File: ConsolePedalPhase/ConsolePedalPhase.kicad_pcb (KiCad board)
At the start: 2 copper layers, 100 x 37 mm, 15 parts, among them J1 Conn_02x25_Counter_Clockwise, Q1 2N3904

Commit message: minor changes
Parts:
- removed D4: 1N914, Diode_SMD:D_SOD-323
- removed Distortion: 250K Distortion, Connector_PinSocket_2.54mm:PinSocket_1x03_P2.54mm_Vertical
- removed Q1: 2N3904, Package_TO_SOT_SMD:SOT-23
- removed REF** (x2): MountingHole_2.5mm_Pad, MountingHole:MountingHole_2.5mm_Pad
- removed Volume: 250K Volume, Connector_PinSocket_2.54mm:PinSocket_1x03_P2.54mm_Vertical
- added C10: 100uF, Capacitor_SMD:C_0603_1608Metric, F.Cu at (137.4, 77.5)
- added C11: 10uF, Capacitor_SMD:C_0603_1608Metric, F.Cu at (133.4, 80.0)
- added C12: 2.2nF, Capacitor_SMD:C_0603_1608Metric, F.Cu at (121.8, 86.1)
- added C13: 1nF, Capacitor_SMD:C_0603_1608Metric, F.Cu at (141.8, 73.6)
- added C14: 10nF, Capacitor_SMD:C_0603_1608Metric, F.Cu at (145.9, 74.4)
- added C15: 470pF, Capacitor_SMD:C_0603_1608Metric, F.Cu at (157.9, 74.8)
- added C16: 100nF, Capacitor_SMD:C_0603_1608Metric, F.Cu at (133.8, 82.5)
- added C17: 4.7nF, Capacitor_SMD:C_0603_1608Metric, F.Cu at (133.8, 85.0)
- added C18: 33nF, Capacitor_SMD:C_0603_1608Metric, F.Cu at (137.4, 80.0)
- added C19: 100nF, Capacitor_SMD:C_0603_1608Metric, F.Cu at (137.8, 82.5)
- added C3: 10nF, Capacitor_SMD:C_0603_1608Metric, F.Cu at (145.8, 87.0)
- added C4: 100nF, Capacitor_SMD:C_0603_1608Metric, F.Cu at (149.8, 84.5)
- added C5: 100uF, Capacitor_SMD:C_0603_1608Metric, F.Cu at (153.9, 74.8)
- added C6: 100nF, Capacitor_SMD:C_0603_1608Metric, F.Cu at (141.8, 71.1)
- added C7: 100nF, Capacitor_SMD:C_0603_1608Metric, F.Cu at (125.8, 86.1)
- added C8: 10nF, Capacitor_SMD:C_0603_1608Metric, F.Cu at (133.4, 77.5)
- added C9: 220nF, Capacitor_SMD:C_0603_1608Metric, F.Cu at (160.7, 56.0)
- added J2: AudioJack2, Connector_Audio:Jack_3.5mm_CUI_SJ1-3535NG_Horizontal, F.Cu at (173.4, 99.7)
- added R10: 470K, Resistor_SMD:R_0603_1608Metric, F.Cu at (141.8, 81.1)
- added R11: 10K, Resistor_SMD:R_0603_1608Metric, F.Cu at (156.8, 69.8)
- added R12: 10K, Resistor_SMD:R_0603_1608Metric, F.Cu at (141.8, 83.6)
- added R13: 22K, Resistor_SMD:R_0603_1608Metric, F.Cu at (145.8, 79.4)
- added R14: 22K, Resistor_SMD:R_0603_1608Metric, F.Cu at (149.9, 76.9)
- added R15: 330K, Resistor_SMD:R_0603_1608Metric, F.Cu at (160.7, 66.0)
- added R16: 330K, Resistor_SMD:R_0603_1608Metric, F.Cu at (153.9, 72.3)
- added R17: 100K, Resistor_SMD:R_0603_1608Metric, F.Cu at (145.8, 82.0)
- added R18: 4.7K, Resistor_SMD:R_0603_1608Metric, F.Cu at (141.8, 86.1)
- added R19: 39K, Resistor_SMD:R_0603_1608Metric, F.Cu at (160.7, 63.5)
- added R20: 100K, Resistor_SMD:R_0603_1608Metric, F.Cu at (160.8, 68.6)
- added R21: 330K, Resistor_SMD:R_0603_1608Metric, F.Cu at (149.9, 74.4)
- added R22: 10K, Resistor_SMD:R_0603_1608Metric, F.Cu at (157.9, 72.3)
- added R23: 100K, Resistor_SMD:R_0603_1608Metric, F.Cu at (149.8, 79.4)
- added R24: 10K, Resistor_SMD:R_0603_1608Metric, F.Cu at (149.8, 82.0)
- added R25: 10K, Resistor_SMD:R_0603_1608Metric, F.Cu at (153.9, 77.4)
- added R4: 100K, Resistor_SMD:R_0603_1608Metric, F.Cu at (152.8, 69.8)
- added R5: 100K, Resistor_SMD:R_0603_1608Metric, F.Cu at (160.7, 61.0)
- added R6: 10K, Resistor_SMD:R_0603_1608Metric, F.Cu at (145.9, 76.9)
- added R7: 4.7K, Resistor_SMD:R_0603_1608Metric, F.Cu at (129.8, 86.1)
- added R8: 100K, Resistor_SMD:R_0603_1608Metric, F.Cu at (145.8, 84.5)
- added R9: 100K, Resistor_SMD:R_0603_1608Metric, F.Cu at (137.8, 85.0)
- added RV1: 20K, Potentiometer_THT:Potentiometer_Alps_RK09L_Single_Vertical, F.Cu at (133.1, 64.8)
- added RV2: C100K, Potentiometer_THT:Potentiometer_Alps_RK09L_Single_Vertical, F.Cu at (118.3, 79.8)
- added RV3: 1M, Potentiometer_THT:Potentiometer_Alps_RK09L_Single_Vertical, F.Cu at (118.3, 64.8)
- added SW1: SW_DPDT_x2, libraries:DPDTSwitch, F.Cu at (152.5, 61.7)
- added U1: TL072, Package_SO:SOIC-8_3.9x4.9mm_P1.27mm, F.Cu at (135.6, 73.0)
- added U2: TL074, Package_SO:SOIC-14_3.9x8.7mm_P1.27mm, F.Cu at (109.8, 81.1)
- added U3: CD4046BE, Package_SO:SOP-16_3.9x9.9mm_P1.27mm, F.Cu at (111.3, 65.4)
- C1: value C -> 100nF
- C2: value C -> 22nF
- D3: value 1N914 -> 1N5817; footprint Diode_SMD:D_SOD-323 -> Diode_SMD:D_SOD-123
- R1: value 2M -> 1M
- R2: value 4.7K -> 1M
- moved R2 58.9 mm to (160.7, 58.5), turned to 0 degrees
- moved C2 35.2 mm to (141.8, 76.1)
- moved R1 31.8 mm to (141.4, 78.6), turned to 0 degrees
- moved D3 24.0 mm to (116.9, 86.5), turned to 0 degrees
- moved R3 16.9 mm to (115.8, 112.6), turned to 90 degrees
- moved D1 11.0 mm to (120.0, 111.8)
- moved D2 9.93 mm to (150.2, 111.8)
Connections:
- C1 pad 2: Net-(C1-Pad2) -> /Input
- C2 pad 2: Net-(C2-Pad2) -> VCO_OUT
- D3 pad 1: Net-(C2-Pad1) -> +9V
- R1 pad 1: Net-(C1-Pad1) -> /Input
- R1 pad 2: Net-(C2-Pad2) -> GND
- R2 pad 1: +9V -> Net-(C1-Pad1)
- R2 pad 2: Net-(C2-Pad2) -> VCC
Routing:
- net Net-(D1-Pad1): track 40.2 -> 0.00 mm
- net /LEDPower: track 90.7 -> 54.1 mm, vias 3 -> 2
- net /Input: track 105.9 -> 71.6 mm
- net /Output: track 92.5 -> 65.8 mm
- net Net-(C1-Pad2): track 22.7 -> 0.00 mm
- net Net-(C2-Pad1): track 21.7 -> 0.00 mm, vias 1 -> 0
- net +9V: track 80.5 -> 60.1 mm
- net GND: track 120.0 -> 102.5 mm, vias 5 -> 4
- net Net-(C1-Pad1): track 8.61 -> 0.00 mm
- net Net-(C2-Pad2): track 6.87 -> 0.00 mm
- removed copper zone on B.Cu, net GND
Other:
- board text added: "Console Pedal Phase V1.0"
- board text removed: "Console Pedal Distortion V1.0"

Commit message: Fixed issues with library loading
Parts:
- added H1: MountingHole_Pad, MountingHole:MountingHole_2.5mm_Pad, F.Cu at (85.3, 122.6)
- added H2: MountingHole_Pad, MountingHole:MountingHole_2.5mm_Pad, F.Cu at (180.2, 122.6)
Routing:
- added copper zone on B.Cu, net GND

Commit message: arranged some of the components on the pcb
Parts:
- moved C9 86.6 mm to (96.5, 114.0)
- moved R2 81.8 mm to (95.8, 108.3), turned to 270 degrees
- moved R11 75.0 mm to (94.2, 111.3), turned to 90 degrees
- moved C5 71.2 mm to (92.7, 111.3), turned to 90 degrees
- moved R20 65.8 mm to (105.7, 104.4)
- moved C6 64.7 mm to (91.2, 111.3), turned to 270 degrees
- moved C15 60.8 mm to (105.7, 105.9)
- moved C4 59.8 mm to (93.5, 104.4)
- moved R1 59.7 mm to (89.2, 107.4), turned to 270 degrees
- moved R6 56.6 mm to (101.6, 112.3), turned to 180 degrees
- moved R17 54.5 mm to (95.8, 103.6), turned to 270 degrees
- moved C10 54.0 mm to (93.5, 109.0), turned to 180 degrees
- moved R12 53.9 mm to (93.5, 107.4), turned to 180 degrees
- moved R8 52.1 mm to (99.8, 109.0)
- moved R23 48.1 mm to (108.7, 104.4), turned to 180 degrees
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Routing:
- net /Input: track 71.6 -> 107.2 mm
- net VCC: track 0.00 -> 17.4 mm
- net Net-(C4-Pad1): track 0.00 -> 13.9 mm, vias 0 -> 2
- net GND: track 102.5 -> 116.0 mm, vias 4 -> 8
- net Net-(C15-Pad1): track 0.00 -> 12.2 mm
- net Net-(C15-Pad2): track 0.00 -> 7.44 mm
- net +9V: track 60.1 -> 65.6 mm
- net CHIP1: track 0.00 -> 4.93 mm
- net Net-(C1-Pad1): track 0.00 -> 3.67 mm
- net Net-(C7-Pad2): track 0.00 -> 3.32 mm
- net /Output: track 65.8 -> 67.4 mm

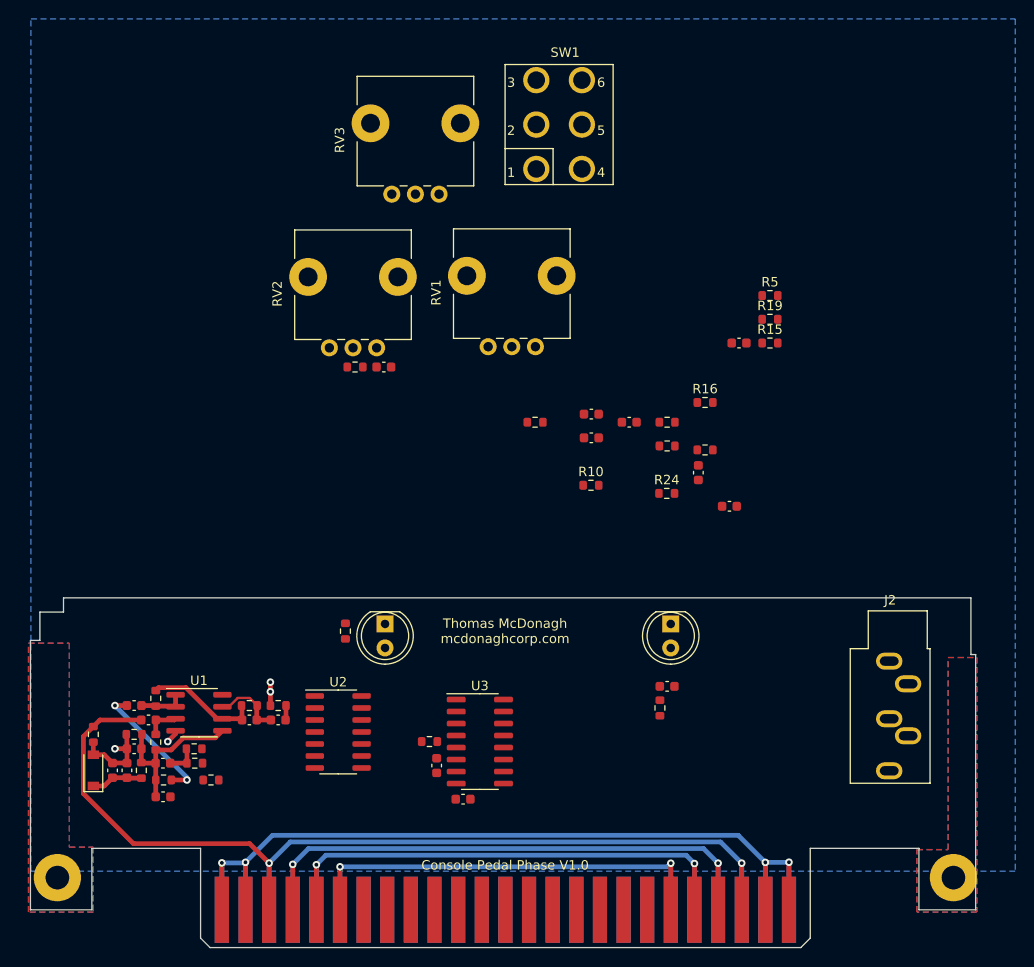
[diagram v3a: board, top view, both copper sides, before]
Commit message: Moved around more parts on pcb. Need to extend top of pcb edge cuts
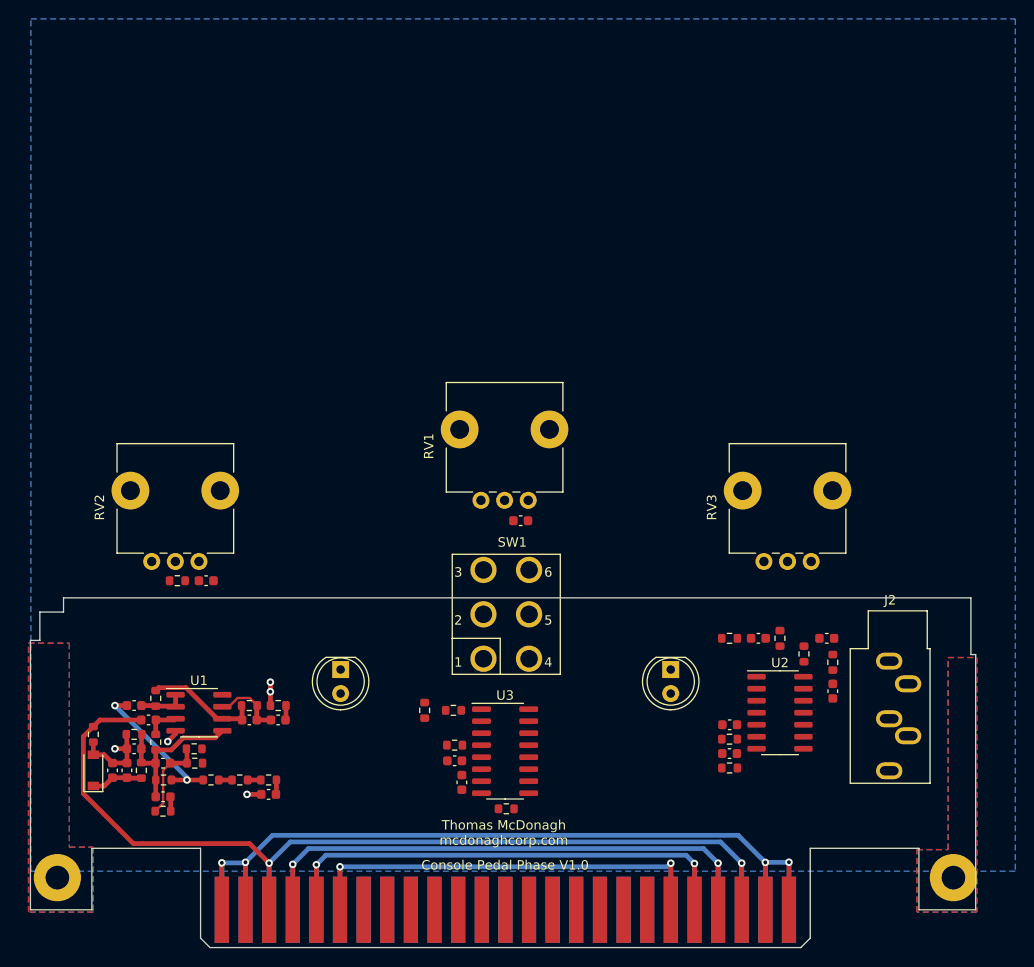
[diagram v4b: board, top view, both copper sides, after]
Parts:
- moved R14 65.9 mm to (96.5, 115.6), turned to 180 degrees
- moved C8 57.5 mm to (107.7, 113.8)
- moved RV3 55.3 mm to (165.1, 89.2)
- moved R5 55.2 mm to (127.3, 104.9)
- moved SW1 52.1 mm to (132.8, 94.7)
- moved R10 48.5 mm to (104.6, 112.3)
- moved R13 47.2 mm to (107.7, 112.3), turned to 180 degrees
- moved U2 46.8 mm to (161.8, 105.2)
- moved R15 45.2 mm to (156.5, 111.0)
- moved C12 43.4 mm to (156.5, 109.5)
- moved R24 37.4 mm to (132.8, 115.3)
- moved C13 36.0 mm to (156.5, 106.4), turned to 180 degrees
- moved R16 35.7 mm to (156.5, 108.0), turned to 180 degrees
- moved R19 33.8 mm to (161.8, 97.3), turned to 270 degrees
- moved C11 29.4 mm to (101.1, 91.2)
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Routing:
- net Net-(C7-Pad2): track 3.32 -> 9.06 mm
- net Net-(C4-Pad1): track 13.9 -> 15.7 mm
- net Net-(C8-Pad2): track 0.00 -> 1.54 mm
- net Net-(C11-Pad1): track 0.00 -> 1.54 mm
- net GND: track 116.0 -> 117.5 mm, vias 8 -> 9
- net Net-(R10-Pad2): track 0.00 -> 1.40 mm
- net Net-(R10-Pad1): track 0.00 -> 1.40 mm

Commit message: Finalizing board. Still need to double check a few things before technically done.
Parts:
- moved R3 29.4 mm to (147.1, 86.4), turned to 0 degrees
- moved J2 28.1 mm to (172.2, 71.6)
- moved D2 11.5 mm to (147.8, 89.4)
- moved D1 11.4 mm to (117.8, 89.4)
- moved RV2 7.42 mm to (107.8, 89.2)
- moved C11 7.37 mm to (108.5, 91.2)
- moved R18 5.59 mm to (103.6, 91.2)
- moved C8 3.05 mm to (104.6, 113.8)
- moved RV3 2.35 mm to (162.8, 89.2)
- moved RV1 1.28 mm to (135.3, 84.0)
- moved C2 1.27 mm to (134.4, 86.1)
- moved R13 1.08 mm to (106.9, 113.0), turned to 90 degrees
- moved R1 0.25 mm to (89.2, 107.2)
- moved SW1 0.09 mm to (132.8, 94.7), turned to 180 degrees
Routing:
- net +9V: track 65.6 -> 171.3 mm, vias 2 -> 7
- net Net-(R10-Pad1): track 1.40 -> 82.8 mm, vias 0 -> 2
- net VCC: track 17.4 -> 95.2 mm, vias 0 -> 3
- net Net-(R10-Pad2): track 1.40 -> 78.1 mm, vias 0 -> 2
- net GND: track 117.5 -> 182.7 mm, vias 9 -> 17
- net /LEDPower: track 54.1 -> 114.9 mm
- net Net-(C8-Pad2): track 1.54 -> 57.9 mm, vias 0 -> 2
- net PH_COMP2_OUT: track 0.00 -> 50.9 mm, vias 0 -> 4
- net Net-(R5-Pad1): track 0.00 -> 48.4 mm, vias 0 -> 2
- net SIG_IN: track 0.00 -> 43.2 mm, vias 0 -> 2
- net Net-(R4-Pad1): track 0.00 -> 39.7 mm, vias 0 -> 3
- net Net-(D1-Pad1): track 0.00 -> 38.7 mm
- net VCO_OUT: track 0.00 -> 36.0 mm
- net Net-(C19-Pad2): track 0.00 -> 32.0 mm
- net COMP_IN: track 0.00 -> 30.3 mm
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- removed copper zone on F.Cu, net GND
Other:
- board size 100 x 37 mm -> 100 x 60 mm

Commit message: minor changes
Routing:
- net GND: track 182.7 -> 184.2 mm, vias 17 -> 18
- added copper zone on F.Cu, net GND
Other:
- board text added: "+"
- board text added: "."
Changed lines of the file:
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@@
   (general
     (thickness 1.6)
-    (drawings 32)
-    (tracks 454)
+    (drawings 36)
+    (tracks 457)
     (zones 0)
     (modules 58)
@@
   (page A4)
   (layers
-    (0 F.Cu signal)
+    (0 F.Cu signal hide)
     (31 B.Cu signal hide)
     (32 B.Adhes user)
@@
     (36 B.SilkS user)
     (37 F.SilkS user)
-    (38 B.Mask user)
-    (39 F.Mask user)
+    (38 B.Mask user hide)
+    (39 F.Mask user hide)
     (40 Dwgs.User user)
     (41 Cmts.User user)
@@
     (mod_text_size 1 1)
     (mod_text_width 0.15)
-    (pad_size 1.8 1.8)
-    (pad_drill 1)
+    (pad_size 5 5)
+    (pad_drill 2.5)
     (pad_to_mask_clearance 0)
     (aux_axis_origin 0 0)
@@
     (descr "TRS 3.5mm, horizontal, through-hole, with switch, https://www.cui.com/product/resource/sj1-353xng.pdf")
     (tags "TRS audio jack stereo horizontal")
-    (fp_text reference J2 (at 0 -3.556) (layer F.SilkS)
+    (fp_text reference J2 (at 2.54 5.588) (layer F.SilkS)
       (effects (font (size 1 1) (thickness 0.15)))
     )
@@
     )
     (pad 1 thru_hole circle (at 0 0) (size 5 5) (drill 2.5) (layers *.Cu *.Mask)
-      (net 1 GND))
+      (net 1 GND) (zone_connect 2))
   )
   (module MountingHole:MountingHole_2.5mm_Pad (layer F.Cu)
@@
     )
     (pad 1 thru_hole circle (at 0 0) (size 5 5) (drill 2.5) (layers *.Cu *.Mask)
-      (net 1 GND))
+      (net 1 GND) (zone_connect 2))
+  )
+  (gr_text . (at 158.496 99.568) (layer F.SilkS)
+    (effects (font (size 1.5 1.5) (thickness 0.3)) (justify mirror))
+  )
+  (gr_text . (at 97.282 101.346) (layer F.SilkS)
+    (effects (font (size 1.5 1.5) (thickness 0.3)) (justify mirror))
+  )
+  (gr_text . (at 129.286 102.87) (layer F.SilkS)
+    (effects (font (size 1.5 1.5) (thickness 0.3)) (justify mirror))
+  )
+  (gr_text + (at 89.154 114.3) (layer F.SilkS)
+    (effects (font (size 1.5 1.5) (thickness 0.3)) (justify mirror))
   )
   (gr_line (start 83.3 70) (end 182 70) (layer Edge.Cuts) (width 0.1))
@@
   (segment (start 165.875 105.156) (end 167.386 103.645) (width 0.5) (layer F.Cu) (net 1))
   (segment (start 164.273 105.156) (end 165.875 105.156) (width 0.5) (layer F.Cu) (net 1))
-  (segment (start 168.643 103.645) (end 168.643 103.645) (width 0.5) (layer F.Cu) (net 1))
   (segment (start 103.873 113.792) (end 102.362 113.792) (width 0.5) (layer F.Cu) (net 1))
   (segment (start 102.362 113.792) (end 102.362 113.792) (width 0.5) (layer F.Cu) (net 1))
@@
   (segment (start 89.154 108.013) (end 89.154 109.602) (width 0.5) (layer F.Cu) (net 1))
   (segment (start 154.78899 115.52699) (end 160.25 120.988) (width 0.5) (layer F.Cu) (net 1))
-  (segment (start 154.78899 106.06901) (end 154.78899 114.45101) (width 0.5) (layer F.Cu) (net 1))
   (segment (start 154.78899 114.45101) (end 154.78899 115.52699) (width 0.5) (layer F.Cu) (net 1))
   (via (at 154.78899 114.45101) (size 0.8) (drill 0.4) (layers F.Cu B.Cu) (net 1))
@@
   (segment (start 146.241 84.899) (end 146.241 84.899) (width 0.5) (layer F.Cu) (net 1))
   (via (at 146.241 84.899) (size 0.8) (drill 0.4) (layers F.Cu B.Cu) (net 1))
+  (segment (start 167.386 103.645) (end 168.897 103.645) (width 0.5) (layer F.Cu) (net 1))
+  (segment (start 168.897 103.645) (end 168.897 103.645) (width 0.5) (layer F.Cu) (net 1))
+  (via (at 168.897 103.645) (size 0.8) (drill 0.4) (layers F.Cu B.Cu) (net 1))
+  (segment (start 154.78899 107.33901) (end 154.78899 114.45101) (width 0.5) (layer F.Cu) (net 1))
+  (segment (start 155.702 106.426) (end 154.78899 107.33901) (width 0.5) (layer F.Cu) (net 1))
   (segment (start 97.728 105.918) (end 97.855 105.791) (width 0.5) (layer F.Cu) (net 2) (status 30))
   (segment (start 95.771 105.918) (end 97.728 105.918) (width 0.5) (layer F.Cu) (net 2) (status 30))
@@
       )
     )
+  )
+  (zone (net 1) (net_name GND) (layer F.Cu) (hatch edge 0.508)
+    (connect_pads (clearance 0))
+    (min_thickness 0.254)
+    (fill yes (arc_segments 32) (thermal_gap 0.508) (thermal_bridge_width 0.508))
+    (polygon
+      (pts
+        (xy 183.388 126.492) (xy 176.276 126.492) (xy 176.276 119.888) (xy 165.608 119.888) (xy 165.608 121.92)
+        (xy 100.076 121.92) (xy 100.076 119.888) (xy 89.408 119.888) (xy 89.408 126.492) (xy 82.296 126.492)
+        (xy 82.296 69.596) (xy 183.388 69.596)
+      )
+    )
